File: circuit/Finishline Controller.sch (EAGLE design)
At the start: 8 parts

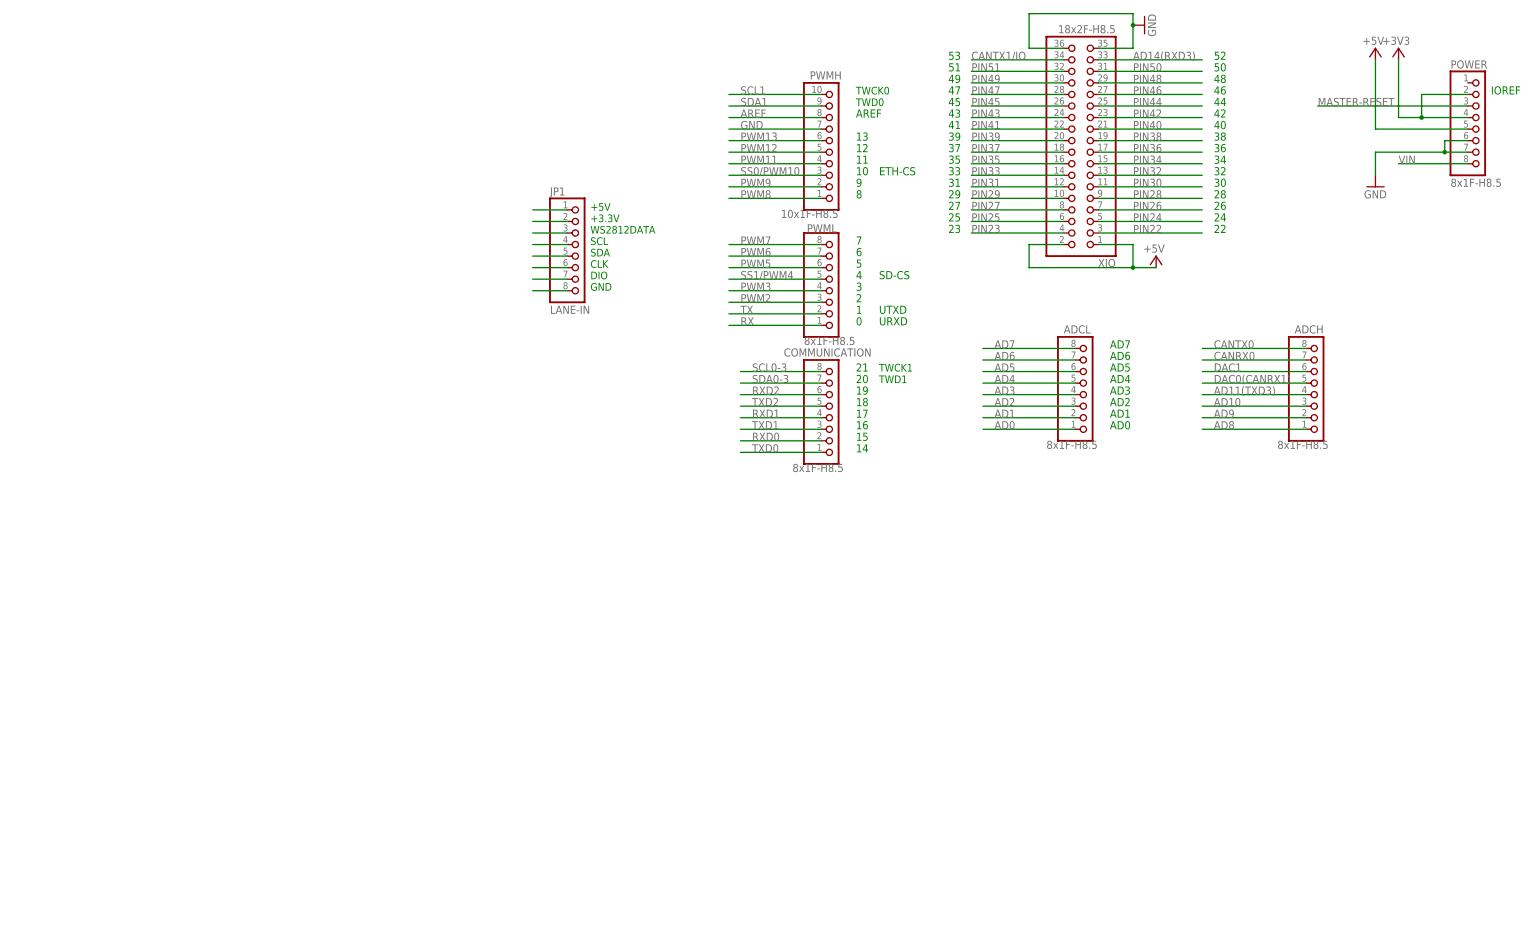
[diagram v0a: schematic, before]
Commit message: add preliminary Due shield
The Due shield has been populated with all components to drive the
display as well as communicate with the start gate electronics.
A prototyping area with THT and SMD pads has been added as well.
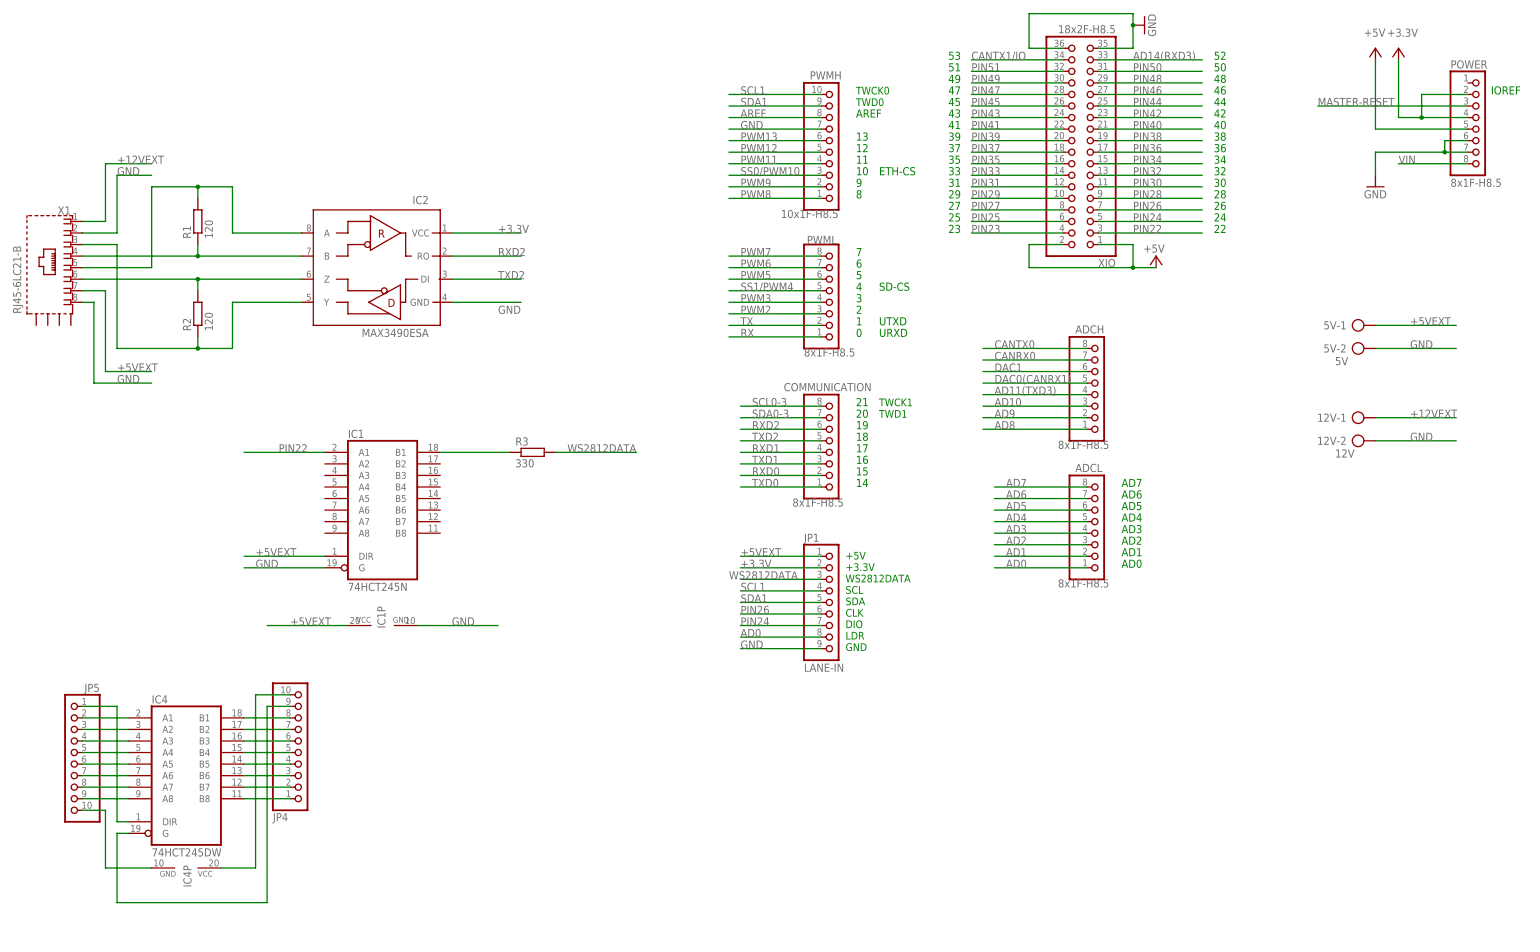
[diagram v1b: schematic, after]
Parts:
- added 12V: 12V, con-ptr500:AK300/2
- added 5V: 5V, con-ptr500:AK300/2
- added IC1: 74HCT245N, 74xx-eu:74HCT245N
- added IC2: MAX3490ESA, miro:MAX3490ESA
- added IC4: 74HCT245DW, 74xx-eu:74HCT245DW
- added JP4, JP5: (no value), pinhead:PINHD-1X10
- added R1, R2: 120, resistor:R-EU_R0805
- added R3: 330, resistor:R-EU_R0805
- added X1: RJ45-6LC21-B, con-tycoelectronics:RJ45-6LC21-B
- JP1: device pinhead:PINHD-1X8 -> pinhead:PINHD-1X9
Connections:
- removed net +3V3: POWER.2, POWER.4
- removed net +5V1: JP1.1
- removed net 0V: JP1.8
- removed net 3.3V: JP1.2
- removed net CLK: JP1.6
- removed net DIO: JP1.7
- removed net SCL: JP1.4
- removed net SDA: JP1.5
- new net +12VEXT: 12V-1.KL, X1.1
- new net +3.3V: IC2.VCC, JP1.2, POWER.2, POWER.4
- new net +5VEXT: 5V-1.KL, IC1A.DIR, IC1P.VCC, JP1.1, X1.7
- new net N$2: IC1A.B1, R3.1
- new net N$3: IC2.B, R1.1, X1.4
- new net N$4: IC2.Z, R2.2, X1.6
- new net N$5: IC2.Y, R2.1, X1.3
- new net N$6: IC2.A, R1.2, X1.5
- new net N$79: IC4A.A1, JP5.2
- new net N$80: IC4A.A2, JP5.3
- new net N$81: IC4A.A3, JP5.4
- new net N$82: IC4A.A4, JP5.5
- new net N$83: IC4A.A5, JP5.6
- new net N$84: IC4A.A6, JP5.7
- new net N$85: IC4A.A7, JP5.8
- new net N$86: IC4A.A8, JP5.9
- new net N$87: IC4P.GND, JP5.10
- new net N$88: IC4A.DIR, JP5.1
- new net N$89: IC4A.B1, JP4.8
- new net N$90: IC4A.B2, JP4.7
- new net N$91: IC4A.B3, JP4.6
- new net N$92: IC4A.B4, JP4.5
- new net N$93: IC4A.B5, JP4.4
- new net N$94: IC4A.B6, JP4.3
- new net N$95: IC4A.B7, JP4.2
- new net N$96: IC4A.B8, JP4.1
- new net N$97: IC4A.G, JP4.9
- new net N$98: IC4P.VCC, JP4.10
- net AD0: now also JP1.8
- net GND: now also 12V-2.KL, 5V-2.KL, IC1A.G, IC1P.GND, IC2.GND, JP1.9, X1.2, X1.8
- net PIN22: now also IC1A.A1
- net PIN24: now also JP1.7
- net PIN26: now also JP1.6
- net RXD2: now also IC2.RO
- net SCL1: now also JP1.4
- net SDA1: now also JP1.5
- net TXD2: now also IC2.DI
- net WS2812DATA: now also R3.2
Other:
- note added: "+5V +3.3V WS2812DATA SCL SDA CLK DIO LDR GND"
- note removed: "+5V +3.3V WS2812DATA SCL SDA CLK DIO GND"
- moved on the sheet: ADCH, ADCL, COMMUNICATION, PWML

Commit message: add mounting holes to the Finishline Display board
New PDFs have been added for the display.
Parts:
- renumbered IC4 to PROTOTYPE
